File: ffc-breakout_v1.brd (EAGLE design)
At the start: 30.5 x 25.1 mm, 5 parts, among them X2 AMP_SFW16R-2STE1LF

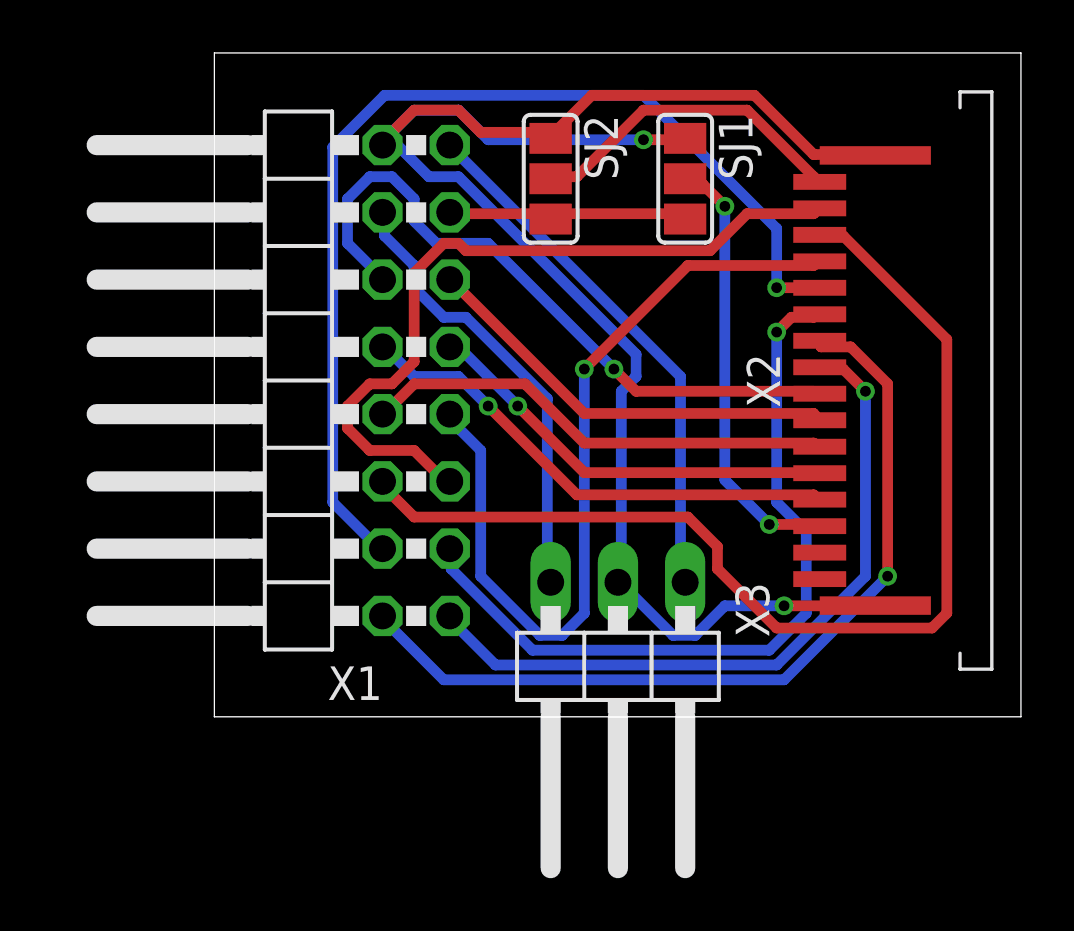
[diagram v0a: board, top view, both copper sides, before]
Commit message: FFC - much better autoroute + cleanup and markup
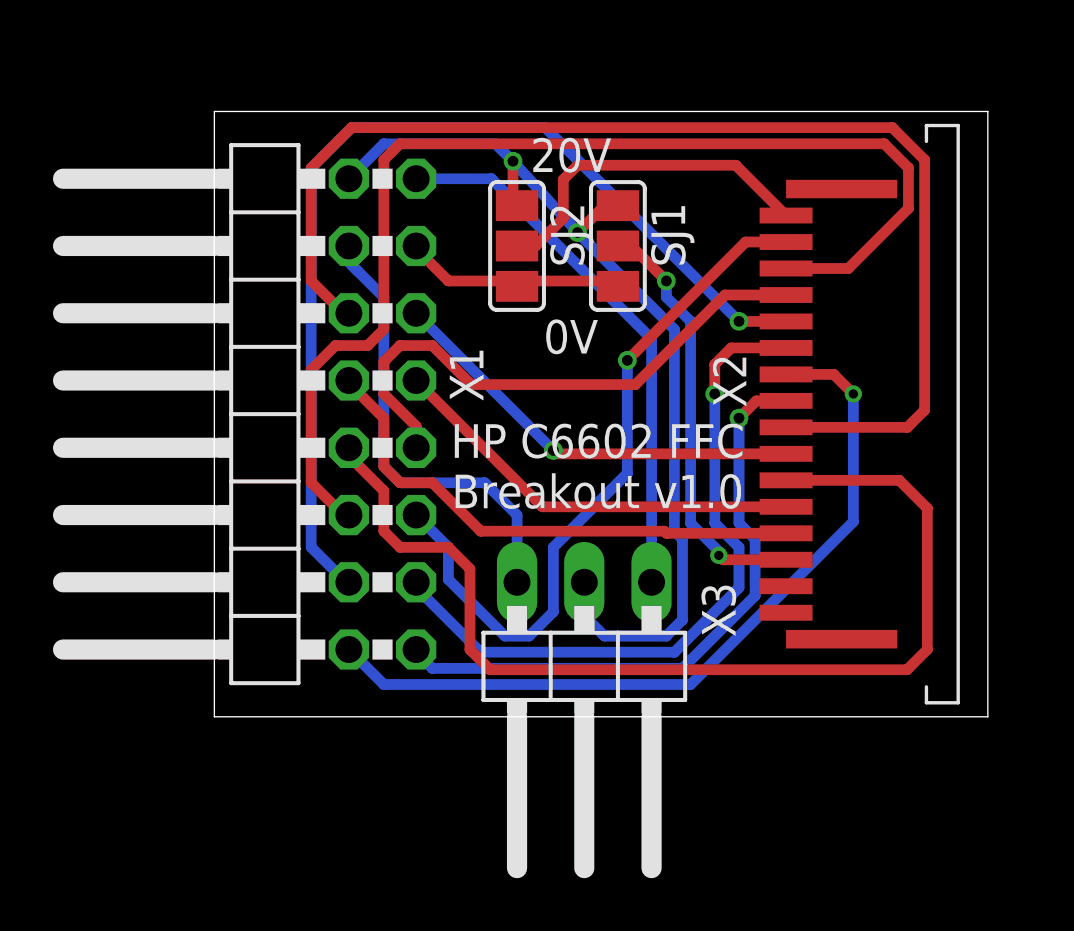
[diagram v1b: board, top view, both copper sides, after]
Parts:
- moved SJ1 3.59 mm to (15.2, 17.8)
- moved SJ2 2.84 mm to (11.4, 17.8)
- moved X1 1.80 mm to (1.27, 11.4)
- moved X2 1.80 mm to (21.6, 11.4)
- moved X3 1.27 mm to (14.0, 1.27)
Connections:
- net N$1: no longer X2.PAD1, X2.PAD2
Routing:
- net N$1: track 66.7 -> 36.2 mm
- net N$14: track 17.9 -> 39.6 mm
- net N$18: track 25.6 -> 45.4 mm, vias 1 -> 0
- net N$13: track 31.6 -> 21.2 mm, vias 1 -> 0
- net N$6: track 27.0 -> 23.3 mm
- net N$9: track 29.0 -> 26.2 mm
- net N$8: track 32.3 -> 29.8 mm
- net N$12: track 41.2 -> 43.5 mm
- net N$11: track 28.6 -> 26.7 mm, vias 0 -> 1
- net N$10: track 39.5 -> 37.9 mm
- net N$16: track 18.9 -> 20.0 mm, vias 1 -> 0
- net N$7: track 12.3 -> 13.1 mm
- net N$3: track 9.22 -> 8.63 mm
- net N$15: vias 1 -> 0
- net N$17: vias 0 -> 1
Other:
- board size 30.5 x 25.1 mm -> 29.2 x 22.9 mm
- board text added: "0V"
- board text added: "20V"
- board text added: "HP C6602 FFC Breakout v1.0"
